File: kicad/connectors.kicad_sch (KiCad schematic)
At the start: 8 parts, among them J10 SSQ-108-01-G-S, J11 SSQ-108-01-G-S, J12 SSQ-108-01-G-S, J13 SSQ-118-01-G-D, J14 SSQ-108-01-G-S, J15 SSQ-108-01-G-S, J16 SSQ-110-01-G-S, J9 SSQ-109-01-G-S

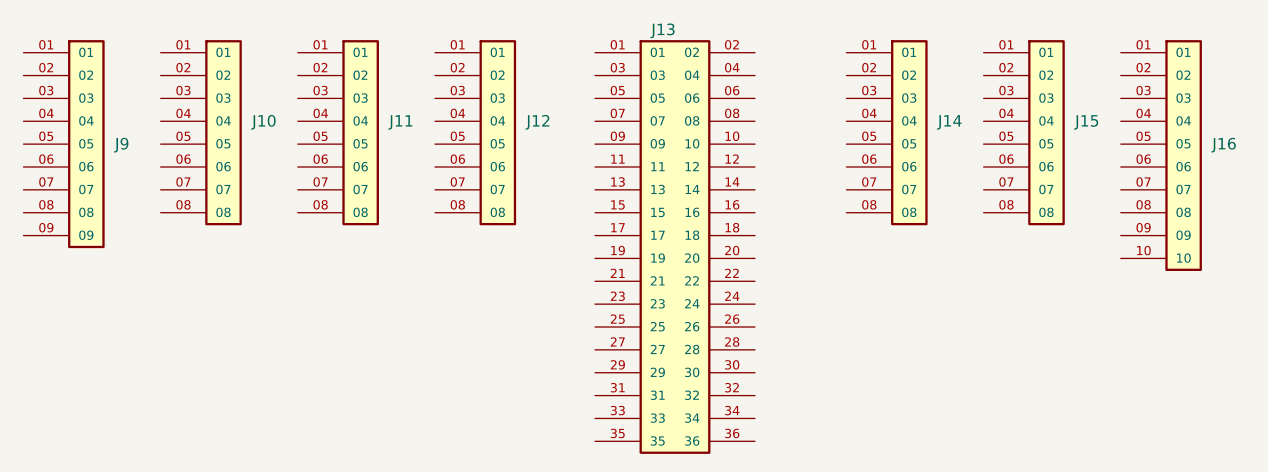
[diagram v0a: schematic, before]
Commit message: Electrical Rules Checker fix
there are still some issues that need to be resolved
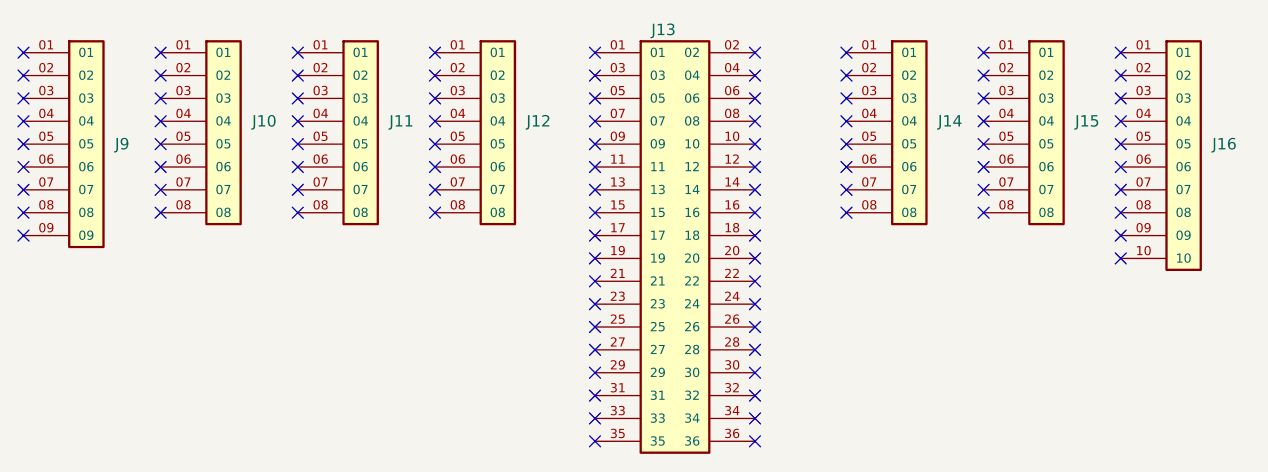
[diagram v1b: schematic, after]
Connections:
- no-connect marks 0 -> 95
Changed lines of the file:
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@@
 (kicad_sch (version 20230121) (generator eeschema)
   (paper "A4")
+  (no_connect (at 183.134 89.154))
+  (no_connect (at 198.374 91.694))
+  (no_connect (at 157.734 119.634))
+  (no_connect (at 157.734 89.154))
+  (no_connect (at 76.454 76.454))
+  (no_connect (at 106.934 78.994))
+  (no_connect (at 157.734 86.614))
+  (no_connect (at 122.174 86.614))
+  (no_connect (at 139.954 81.534))
+  (no_connect (at 167.894 81.534))
+  (no_connect (at 183.134 86.614))
+  (no_connect (at 76.454 78.994))
+  (no_connect (at 198.374 96.774))
+  (no_connect (at 91.694 89.154))
+  (no_connect (at 91.694 86.614))
+  (no_connect (at 139.954 76.454))
+  (no_connect (at 139.954 104.394))
+  (no_connect (at 157.734 106.934))
+  (no_connect (at 183.134 94.234))
+  (no_connect (at 139.954 101.854))
+  (no_connect (at 122.174 78.994))
+  (no_connect (at 91.694 94.234))
+  (no_connect (at 198.374 99.314))
+  (no_connect (at 106.934 84.074))
+  (no_connect (at 183.134 78.994))
+  (no_connect (at 106.934 81.534))
+  (no_connect (at 183.134 91.694))
+  (no_connect (at 122.174 84.074))
+  (no_connect (at 157.734 114.554))
+  (no_connect (at 139.954 89.154))
+  (no_connect (at 139.954 114.554))
+  (no_connect (at 76.454 94.234))
+  (no_connect (at 157.734 112.014))
+  (no_connect (at 76.454 86.614))
+  (no_connect (at 122.174 81.534))
+  (no_connect (at 157.734 84.074))
+  (no_connect (at 76.454 84.074))
+  (no_connect (at 198.374 78.994))
+  (no_connect (at 139.954 86.614))
+  (no_connect (at 157.734 101.854))
+  (no_connect (at 106.934 94.234))
+  (no_connect (at 183.134 76.454))
+  (no_connect (at 106.934 89.154))
+  (no_connect (at 167.894 84.074))
+  (no_connect (at 139.954 94.234))
+  (no_connect (at 167.894 76.454))
+  (no_connect (at 91.694 81.534))
+  (no_connect (at 157.734 76.454))
+  (no_connect (at 167.894 86.614))
+  (no_connect (at 76.454 81.534))
+  (no_connect (at 198.374 81.534))
+  (no_connect (at 167.894 89.154))
+  (no_connect (at 139.954 96.774))
+  (no_connect (at 139.954 78.994))
+  (no_connect (at 122.174 94.234))
+  (no_connect (at 198.374 84.074))
+  (no_connect (at 139.954 117.094))
+  (no_connect (at 167.894 78.994))
+  (no_connect (at 139.954 109.474))
+  (no_connect (at 139.954 119.634))
+  (no_connect (at 157.734 78.994))
+  (no_connect (at 139.954 106.934))
+  (no_connect (at 198.374 94.234))
+  (no_connect (at 76.454 91.694))
+  (no_connect (at 106.934 76.454))
+  (no_connect (at 167.894 94.234))
+  (no_connect (at 139.954 91.694))
+  (no_connect (at 139.954 99.314))
+  (no_connect (at 106.934 86.614))
+  (no_connect (at 183.134 84.074))
+  (no_connect (at 139.954 84.074))
+  (no_connect (at 198.374 86.614))
+  (no_connect (at 157.734 99.314))
+  (no_connect (at 91.694 91.694))
+  (no_connect (at 139.954 112.014))
+  (no_connect (at 157.734 117.094))
+  (no_connect (at 183.134 81.534))
+  (no_connect (at 122.174 76.454))
+  (no_connect (at 76.454 89.154))
+  (no_connect (at 91.694 76.454))
+  (no_connect (at 122.174 91.694))
+  (no_connect (at 106.934 91.694))
+  (no_connect (at 157.734 81.534))
+  (no_connect (at 157.734 109.474))
+  (no_connect (at 157.734 91.694))
+  (no_connect (at 91.694 78.994))
+  (no_connect (at 198.374 89.154))
+  (no_connect (at 198.374 76.454))
+  (no_connect (at 76.454 96.774))
+  (no_connect (at 157.734 94.234))
+  (no_connect (at 167.894 91.694))
+  (no_connect (at 91.694 84.074))
+  (no_connect (at 157.734 96.774))
+  (no_connect (at 122.174 89.154))
+  (no_connect (at 157.734 104.394))
   (symbol (lib_id "SSQ-108-01-G-S:SSQ-108-01-G-S") (at 172.974 84.074 0) (unit 1)
     (in_bom yes) (on_board no) (dnp no)
@@
       (effects (font (size 1.27 1.27)) hide)
     )
+    (property "Sim.Enable" "0" (at 172.974 84.074 0)
+      (effects (font (size 1.27 1.27)) hide)
+    )
     (pin "01")
     (pin "02")
@@
       (effects (font (size 1.27 1.27)) hide)
     )
+    (property "Sim.Enable" "0" (at 96.774 84.074 0)
+      (effects (font (size 1.27 1.27)) hide)
+    )
     (pin "01")
     (pin "02")
@@
       (effects (font (size 1.27 1.27)) hide)
     )
+    (property "Sim.Enable" "0" (at 188.214 84.074 0)
+      (effects (font (size 1.27 1.27)) hide)
+    )
     (pin "01")
     (pin "02")
@@
     )
     (property "SPN" "SAM1179-18-ND" (at 148.844 99.314 0)
+      (effects (font (size 1.27 1.27)) hide)
+    )
+    (property "Sim.Enable" "0" (at 148.844 99.314 0)
       (effects (font (size 1.27 1.27)) hide)
     )
@@
       (effects (font (size 1.27 1.27)) hide)
     )
+    (property "Sim.Enable" "0" (at 112.014 84.074 0)
+      (effects (font (size 1.27 1.27)) hide)
+    )
     (pin "01")
     (pin "02")
@@
       (effects (font (size 1.27 1.27)) hide)
     )
+    (property "Sim.Enable" "0" (at 81.534 86.614 0)
+      (effects (font (size 1.27 1.27)) hide)
+    )
     (pin "01")
     (pin "02")
@@
       (effects (font (size 1.27 1.27)) hide)
     )
+    (property "Sim.Enable" "0" (at 203.454 89.154 0)
+      (effects (font (size 1.27 1.27)) hide)
+    )
     (pin "01")
     (pin "02")
@@
       (effects (font (size 1.27 1.27)) hide)
     )
+    (property "Sim.Enable" "0" (at 127.254 84.074 0)
+      (effects (font (size 1.27 1.27)) hide)
+    )
